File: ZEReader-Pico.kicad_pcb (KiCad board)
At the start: 2 copper layers, 100 x 110 mm, 73 parts, among them J1 Micro_SD_Card_Det2, J2 UART, J3 SWD, J4 Conn_01x24_MountingPin, J5 UJ20-C-H-G-SMT-TR, J6 Conn_01x02_Socket, Q1 Si1308EDL, Q2 DMG2305UX-7, SW1 SW_Push, SW2 SW_Push, SW3 SW_Push, SW4 SW_Push, U1 Pico, U2 BQ24090DGQ

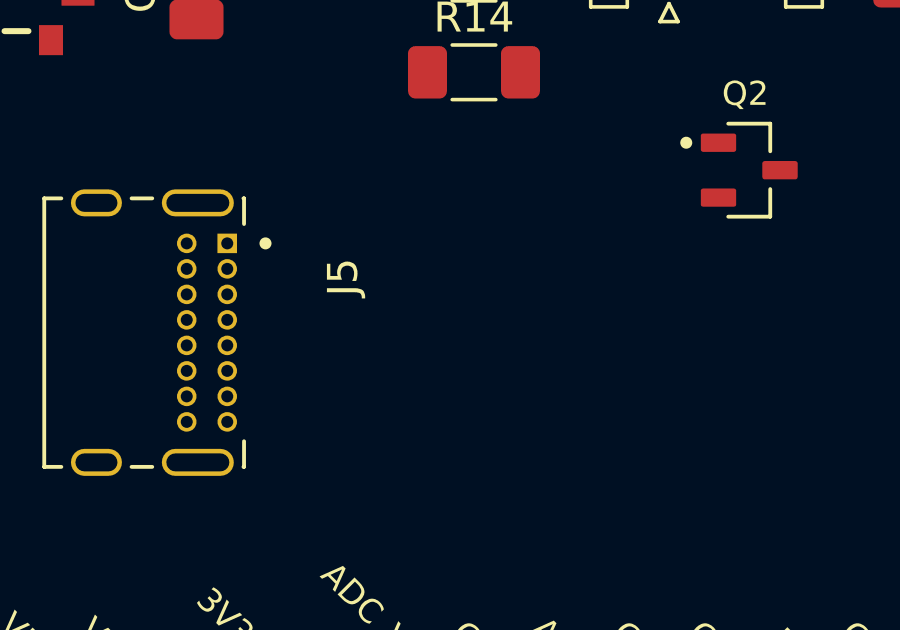
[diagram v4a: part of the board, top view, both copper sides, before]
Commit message: Added CC line pulldown resistors
Signed-off-by: Anna-Lena Marx <anna-lena.marx@web.de>
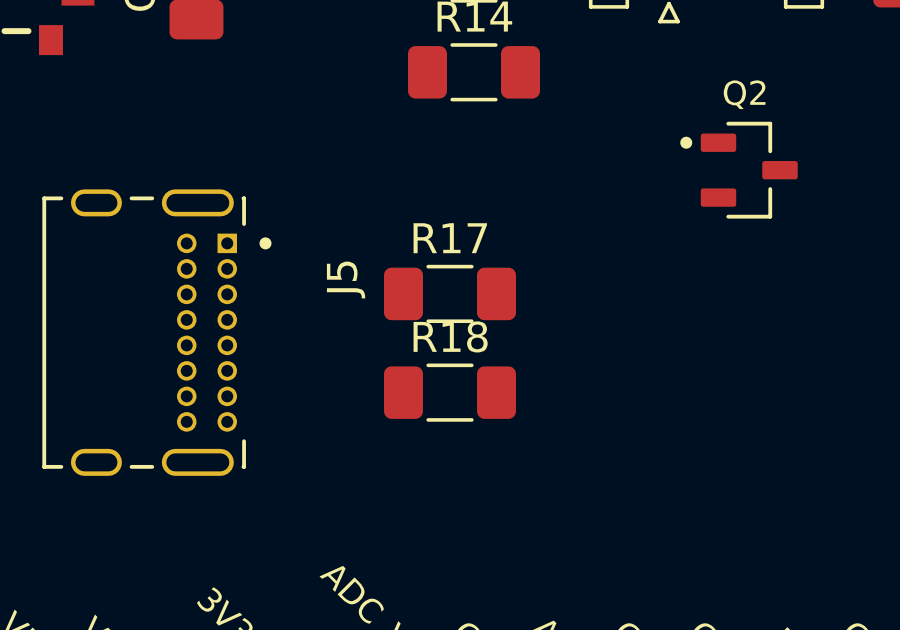
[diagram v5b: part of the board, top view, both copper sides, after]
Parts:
- added R17: 5.1k, Resistor_SMD:R_1206_3216Metric_Pad1.30x1.75mm_HandSolder, F.Cu at (66.5, 62.7)
- added R18: 5.1k, Resistor_SMD:R_1206_3216Metric_Pad1.30x1.75mm_HandSolder, F.Cu at (66.5, 66.0)
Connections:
- J5 pad A5: unconnected-(J5-CC1-PadA5) -> Net-(J5-CC1)
- J5 pad B5: unconnected-(J5-CC2-PadB5) -> Net-(J5-CC2)
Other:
- board text added: "v1-$(REF)"

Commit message: Add 3rd party symbols, footprints and 3d models to make the repo self-contained
Signed-off-by: Anna-Lena Marx <anna-lena.marx@web.de>
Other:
- board text added: "v1 Git Rev: ${kibot_git-hash}"
- board text removed: "v1-$(REF)"
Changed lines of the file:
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@@
 		(tags "test point plated hole")
 		(property "Reference" "TP2_EPD_RST1"
-			(at 0 -2.498 360)
+			(at 0 -2.498 0)
 			(layer "F.SilkS")
 			(effects
@@
 		)
 		(property "Value" "EPD_RST"
-			(at 0 2.45 360)
+			(at 0 2.45 0)
 			(layer "F.Fab")
 			(effects
@@
 		)
 		(fp_text user "${REFERENCE}"
-			(at 0 -2.5 360)
+			(at 0 -2.5 0)
 			(layer "F.Fab")
 			(effects
@@
 		(tags "test point plated hole")
 		(property "Reference" "TP1_EPD_BUSY1"
-			(at 0 -2.498 360)
+			(at 0 -2.498 0)
 			(layer "F.SilkS")
 			(effects
@@
 		)
 		(property "Value" "EPD_BUSY"
-			(at 0 2.45 360)
+			(at 0 2.45 0)
 			(layer "F.Fab")
 			(effects
@@
 		)
 		(fp_text user "${REFERENCE}"
-			(at 0 -2.5 360)
+			(at 0 -2.5 0)
 			(layer "F.Fab")
 			(effects
@@
 		(tags "test point plated hole")
 		(property "Reference" "TP3_EPD_DC1"
-			(at 0 -2.498 360)
+			(at 0 -2.498 0)
 			(layer "F.SilkS")
 			(effects
@@
 		)
 		(property "Value" "EPD_DC"
-			(at 0 2.45 360)
+			(at 0 2.45 0)
 			(layer "F.Fab")
 			(effects
@@
 		)
 		(fp_text user "${REFERENCE}"
-			(at 0 -2.5 360)
+			(at 0 -2.5 0)
 			(layer "F.Fab")
 			(effects
@@
 			)
 		)
-		(model "/Users/anna/Downloads/BQ24092DGQR.STEP"
+		(model "${KIPRJMOD}/packages3d/BQ24092DGQR.STEP"
 			(offset
 				(xyz 0 0 0)
@@
 		(tags "test point plated hole")
 		(property "Reference" "TP4_EPD_CS1"
-			(at 0 -2.498 360)
+			(at 0 -2.498 0)
 			(layer "F.SilkS")
 			(effects
@@
 		)
 		(property "Value" "EPD_CS"
-			(at 0 2.45 360)
+			(at 0 2.45 0)
 			(layer "F.Fab")
 			(effects
@@
 		)
 		(fp_text user "${REFERENCE}"
-			(at 0 -2.5 360)
+			(at 0 -2.5 0)
 			(layer "F.Fab")
 			(effects
@@
 		(tags "test point plated hole")
 		(property "Reference" "TP10_SD_DO1"
-			(at 0 -2.498 360)
+			(at 0 -2.498 0)
 			(layer "F.SilkS")
 			(effects
@@
 		)
 		(property "Value" "SD_DO"
-			(at 0 2.45 360)
+			(at 0 2.45 0)
 			(layer "F.Fab")
 			(effects
@@
 		)
 		(fp_text user "${REFERENCE}"
-			(at 0 -2.5 360)
+			(at 0 -2.5 0)
 			(layer "F.Fab")
 			(effects
@@
 		(tags "test point plated hole")
 		(property "Reference" "TP5_EPD_SCK1"
-			(at 0 -2.498 360)
+			(at 0 -2.498 0)
 			(layer "F.SilkS")
 			(effects
@@
 		)
 		(property "Value" "EPD_SCK"
-			(at 0 2.45 360)
+			(at 0 2.45 0)
 			(layer "F.Fab")
 			(effects
@@
 		)
 		(fp_text user "${REFERENCE}"
-			(at 0 -2.5 360)
+			(at 0 -2.5 0)
 			(layer "F.Fab")
 			(effects
@@
 			(solder_mask_margin 0.102)
 		)
-		(model "/Users/anna/Downloads/450404015514/4504040015514.pretty/450404015514.step"
+		(model "${KIPRJMOD}/packages3d/450404015514.step"
 			(offset
 				(xyz 0 0 0)
@@
 		(tags "test point plated hole")
 		(property "Reference" "TP7_GND1"
-			(at 0 -2.498 360)
+			(at 0 -2.498 0)
 			(layer "F.SilkS")
 			(effects
@@
 		)
 		(property "Value" "GND"
-			(at 0 2.45 360)
+			(at 0 2.45 0)
 			(layer "F.Fab")
 			(effects
@@
 		)
 		(fp_text user "${REFERENCE}"
-			(at 0 -2.5 360)
+			(at 0 -2.5 0)
 			(layer "F.Fab")
 			(effects
@@
 		(tags "test point plated hole")
 		(property "Reference" "TP6_EPD_DIN1"
-			(at 0 -2.498 360)
+			(at 0 -2.498 0)
 			(layer "F.SilkS")
 			(effects
@@
 		)
 		(property "Value" "EPD_DIN"
-			(at 0 2.45 360)
+			(at 0 2.45 0)
 			(layer "F.Fab")
 			(effects
@@
 		)
 		(fp_text user "${REFERENCE}"
-			(at 0 -2.5 360)
+			(at 0 -2.5 0)
 			(layer "F.Fab")
 			(effects
@@
 			(solder_mask_margin 0.102)
 		)
-		(model "/Users/anna/Downloads/450404015514/4504040015514.pretty/450404015514.step"
+		(model "${KIPRJMOD}/packages3d/450404015514.step"
 			(offset
 				(xyz 0 0 0)
@@
 			)
 			(rotate
-				(xyz 180 180 0)
+				(xyz -180 -180 0)
 			)
 		)
@@
 			(solder_mask_margin 0.102)
 		)
-		(model "/Users/anna/Downloads/UJ20-C-H-G-SMT-TR/UJ20.pretty/UJ20-C-H-G-SMT-TR.step"
+		(model "${KIPRJMOD}/packages3d/UJ20-C-H-G-SMT-TR.step"
 			(offset
 				(xyz 0 -4 0)
@@
 			(pintype "bidirectional")
 		)
-		(model "/Users/anna/Downloads/KiCad-RP-Pico-main/RP-Pico Libraries/Pico.wrl"
+		(model "${KIPRJMOD}/packages3d/Pico.wrl"
 			(offset
 				(xyz 0 0 0)
@@
 		(layer "Edge.Cuts")
 	)
-	(gr_text "v1-$(REF)"
+	(gr_text "v1\nGit Rev: ${kibot_git-hash}"
 		(at 125 89 0)
 		(layer "B.SilkS")

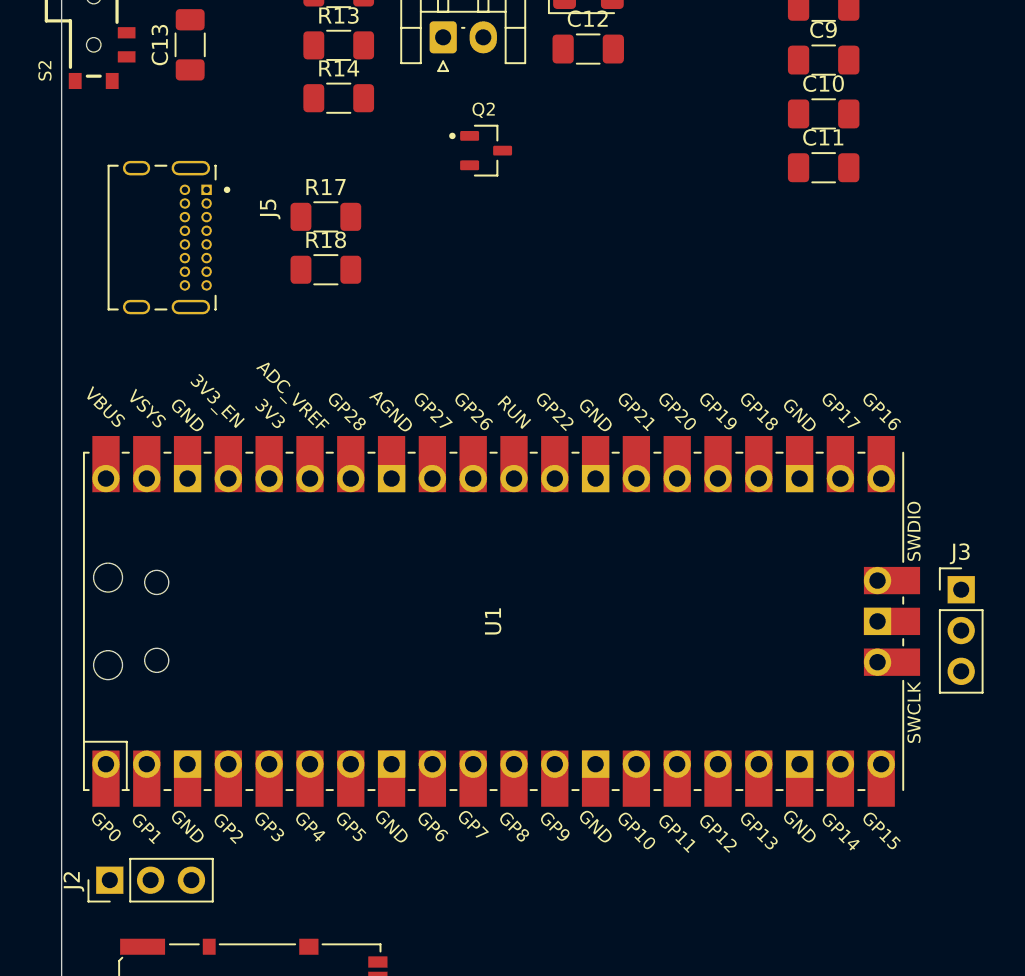
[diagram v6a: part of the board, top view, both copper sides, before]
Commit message: fix selfcontainment issues, added 2D rendering
Signed-off-by: Anna-Lena Marx <anna-lena.marx@web.de>
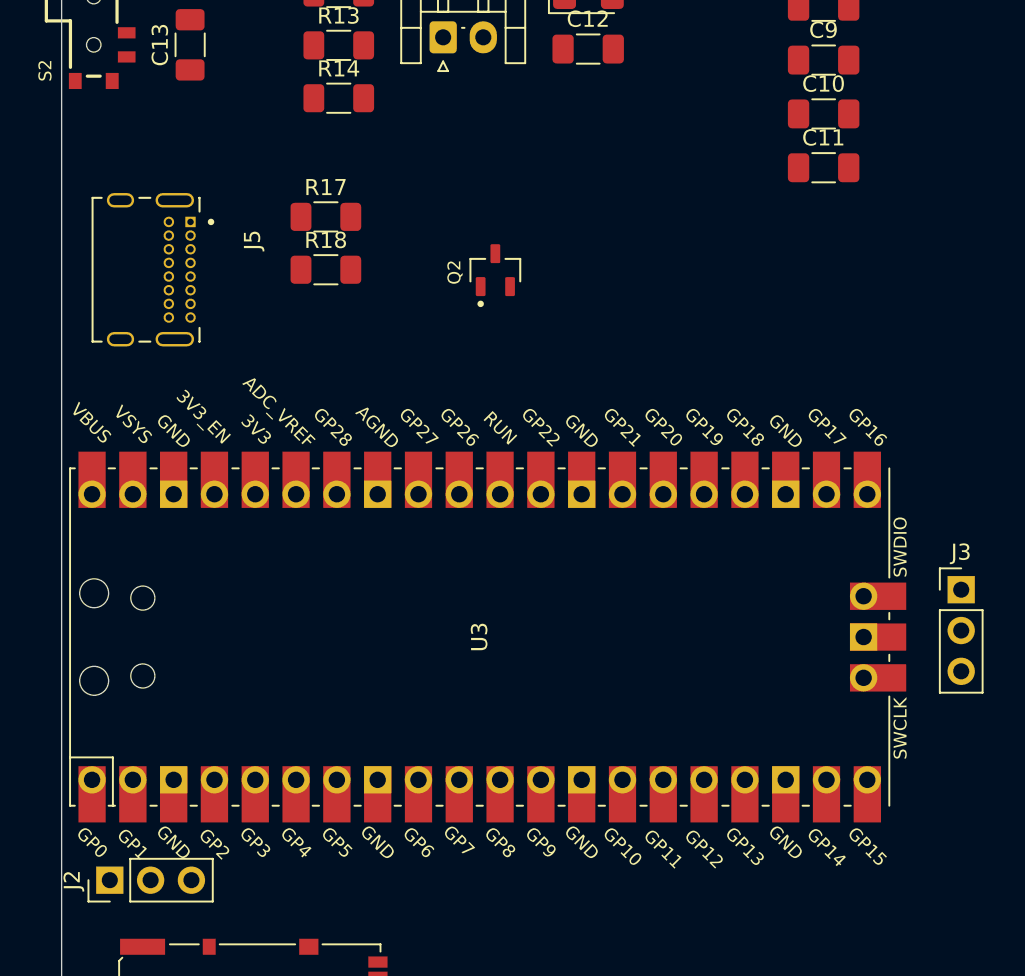
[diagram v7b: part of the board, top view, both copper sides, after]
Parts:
- removed U1: Pico, RPi_Pico:RPi_Pico_SMD_TH
- added U3: Pico, prj-footprints:RPi_Pico_SMD_TH, F.Cu at (76.0, 88.9)
- J5: footprint UJ20:CUI_UJ20-C-H-G-SMT-TR -> prj-footprints:CUI_UJ20-C-H-G-SMT-TR
- L1: footprint footprints:IND_IFSC_1515AH_VIS-L -> prj-footprints:IND_IFSC_1515AH_VIS-L
- Q2: footprint Package_TO_SOT_SMD:SOT91P240X110-3N_DMG2305UX-7 -> prj-footprints:SOT91P240X110-3N_DMG2305UX-7
- moved Q2 7.46 mm to (77.0, 66.0), turned to 90 degrees
- moved J5 2.24 mm to (54.0, 66.0)

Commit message: selfcontaining, KiBot output
Signed-off-by: Anna-Lena Marx <anna-lena.marx@web.de>
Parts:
- S1, S2: footprint 4504040015514:450404015514 -> prj-footprints:450404015514
- moved J5 1.37 mm to (55.3, 66.3)
